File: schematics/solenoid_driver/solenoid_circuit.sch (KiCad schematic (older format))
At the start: 10 parts, among them Q1 Q_NPN_CBE, Q2 Q_PNP_CBE, Q3 Q_NMOS_GDS, U2 SFH617A-1

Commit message: created mtrix_controller project, updated schematic on solenoid_driver
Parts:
- D1: value D_Schottky -> 1n5819
- Q1: value Q_NPN_CBE -> 2n3904
- Q2: value Q_PNP_CBE -> 2n3906
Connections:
- net labels added: +3.3V, Sig_in
- wire segments 34 -> 35
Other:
- moved on the sheet: R1
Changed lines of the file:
@@
 	5150 3300 5300 3300
 Wire Wire Line
-	5300 3100 5050 3100
+	5300 2400 5300 2650
 $Comp
 L Device:R R1
 U 1 1 613B2B01
-P 4900 3100
-F 0 "R1" V 4693 3100 50  0000 C CNN
-F 1 "R" V 4784 3100 50  0000 C CNN
-F 2 "" V 4830 3100 50  0001 C CNN
-F 3 "~" H 4900 3100 50  0001 C CNN
-	1    4900 3100
-	0    1    1    0
-$EndComp
-Wire Wire Line
-	4600 3100 4750 3100
+P 5300 2800
+F 0 "R1" V 5093 2800 50  0000 C CNN
+F 1 "R" V 5184 2800 50  0000 C CNN
+F 2 "" V 5230 2800 50  0001 C CNN
+F 3 "~" H 5300 2800 50  0001 C CNN
+	1    5300 2800
+	1    0    0    -1
+$EndComp
+Wire Wire Line
+	5300 3100 5300 2950
 $Comp
 L power:GND #PWR010
@@
 P 7000 2600
 F 0 "Q1" H 7191 2646 50  0000 L CNN
-F 1 "Q_NPN_CBE" H 7191 2555 50  0000 L CNN
+F 1 "2n3904" H 7200 2550 50  0000 L CNN
 F 2 "" H 7200 2700 50  0001 C CNN
 F 3 "~" H 7000 2600 50  0001 C CNN
@@
 P 7000 3100
 F 0 "Q2" H 7190 3054 50  0000 L CNN
-F 1 "Q_PNP_CBE" H 7190 3145 50  0000 L CNN
+F 1 "2n3906" H 7190 3145 50  0000 L CNN
 F 2 "" H 7200 3200 50  0001 C CNN
 F 3 "~" H 7000 3100 50  0001 C CNN
@@
 U 1 1 613B2B48
 P 7600 2850
-F 0 "R4" V 7393 2850 50  0000 C CNN
-F 1 "R" V 7484 2850 50  0000 C CNN
+F 0 "R4" V 7500 2900 50  0000 C CNN
+F 1 "R" V 7700 2900 50  0000 C CNN
 F 2 "" V 7530 2850 50  0001 C CNN
 F 3 "~" H 7600 2850 50  0001 C CNN
@@
 Wire Wire Line
 	8150 3050 8150 3550
-Wire Wire Line
-	7850 2850 7800 2850
 $Comp
 L Device:L_Core_Ferrite L1
@@
 P 8950 2200
 F 0 "D1" V 8904 2280 50  0000 L CNN
-F 1 "D_Schottky" V 8995 2280 50  0000 L CNN
+F 1 "1n5819" V 8995 2280 50  0000 L CNN
 F 2 "" H 8950 2200 50  0001 C CNN
 F 3 "~" H 8950 2200 50  0001 C CNN
@@
 Text Notes 4300 1750 0    50   ~ 0
 Solenoid driver circuit: \nmosfet push-pull circuit
+Wire Wire Line
+	7750 2850 7850 2850
+$Comp
+L power:+3.3V #PWR?
+U 1 1 614B4CD8
+P 5300 2400
+F 0 "#PWR?" H 5300 2250 50  0001 C CNN
+F 1 "+3.3V" H 5315 2573 50  0000 C CNN
+F 2 "" H 5300 2400 50  0001 C CNN
+F 3 "" H 5300 2400 50  0001 C CNN
+	1    5300 2400
+	1    0    0    -1
+$EndComp
+Wire Wire Line
+	4700 3100 5300 3100
+Connection ~ 5300 3100
+Text HLabel 4700 3100 0    50   Input ~ 0
+Sig_in
 $EndSCHEMATC

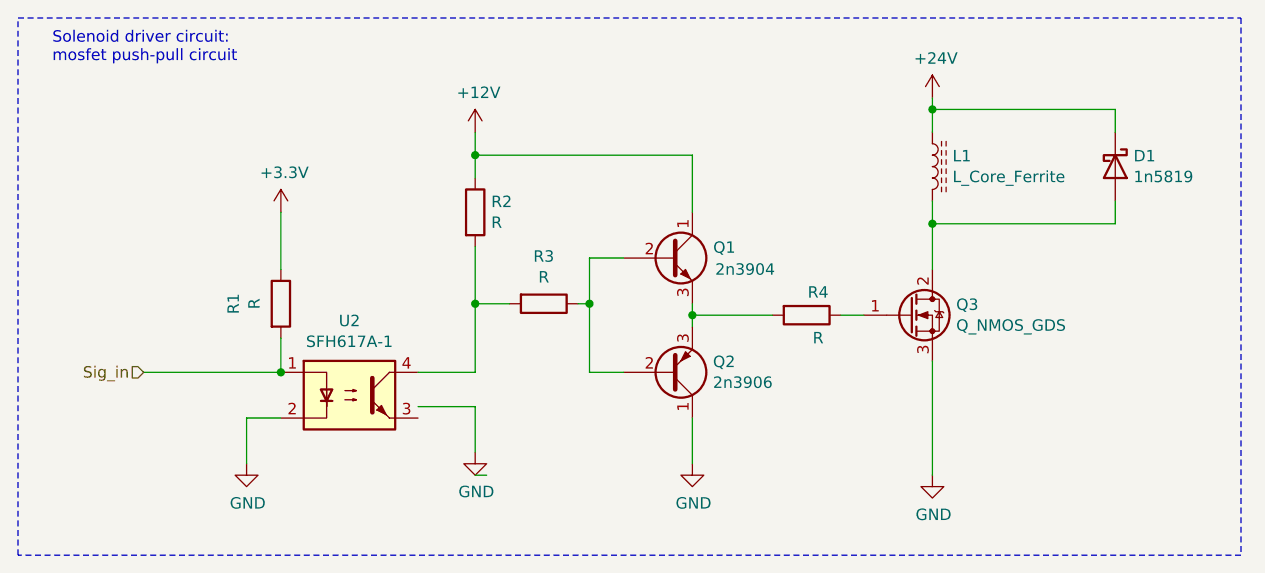
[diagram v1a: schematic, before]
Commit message: updated schematic: resistor value, added workspace for Waveforms Electronics Explorer
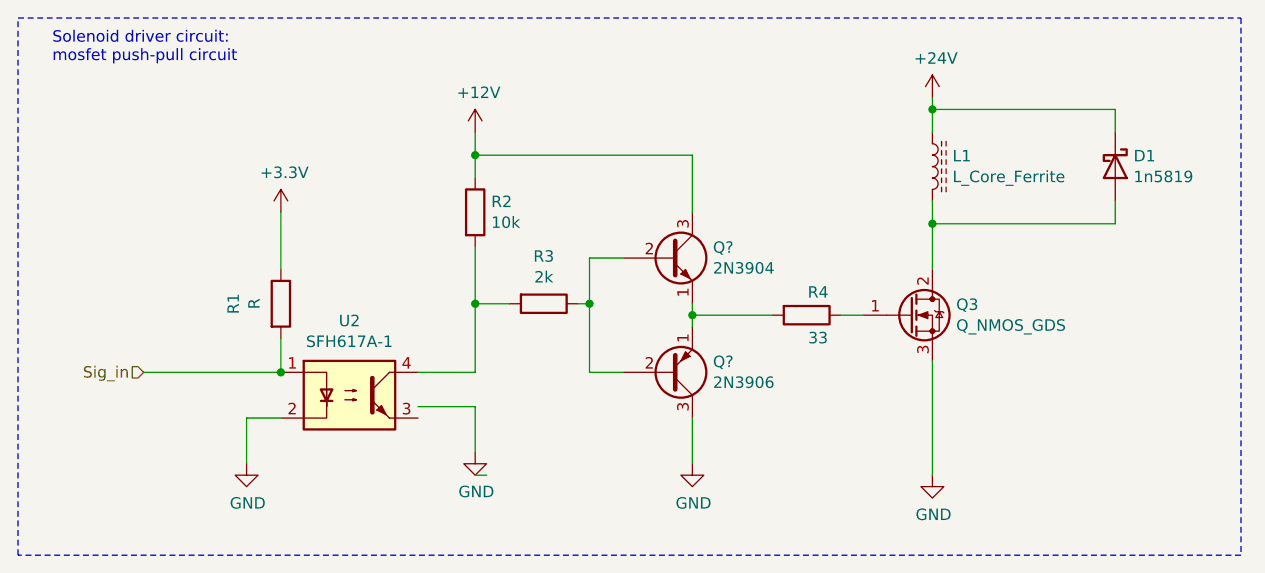
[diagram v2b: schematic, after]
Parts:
- removed Q1: 2n3904, symbol Device:Q_NPN_CBE
- removed Q2: 2n3906, symbol Device:Q_PNP_CBE
- added Q?: 2N3904, symbol Device:Q_NPN_EBC
- added Q?: 2N3906, symbol Device:Q_PNP_EBC
- R2: value R -> 10k
- R3: value R -> 2k
- R4: value R -> 33
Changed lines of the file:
@@
 P 6150 2400
 F 0 "R2" H 6220 2446 50  0000 L CNN
-F 1 "R" H 6220 2355 50  0000 L CNN
+F 1 "10k" H 6220 2355 50  0000 L CNN
 F 2 "" V 6080 2400 50  0001 C CNN
 F 3 "~" H 6150 2400 50  0001 C CNN
@@
 P 6450 2800
 F 0 "R3" V 6243 2800 50  0000 C CNN
-F 1 "R" V 6334 2800 50  0000 C CNN
+F 1 "2k" V 6334 2800 50  0000 C CNN
 F 2 "" V 6380 2800 50  0001 C CNN
 F 3 "~" H 6450 2800 50  0001 C CNN
 	1    6450 2800
 	0    1    1    0
-$EndComp
-$Comp
-L Device:Q_NPN_CBE Q1
-U 1 1 613B2B26
-P 7000 2600
-F 0 "Q1" H 7191 2646 50  0000 L CNN
-F 1 "2n3904" H 7200 2550 50  0000 L CNN
-F 2 "" H 7200 2700 50  0001 C CNN
-F 3 "~" H 7000 2600 50  0001 C CNN
-	1    7000 2600
-	1    0    0    -1
-$EndComp
-$Comp
-L Device:Q_PNP_CBE Q2
-U 1 1 613B2B2C
-P 7000 3100
-F 0 "Q2" H 7190 3054 50  0000 L CNN
-F 1 "2n3906" H 7190 3145 50  0000 L CNN
-F 2 "" H 7200 3200 50  0001 C CNN
-F 3 "~" H 7000 3100 50  0001 C CNN
-	1    7000 3100
-	1    0    0    1
 $EndComp
 Wire Wire Line
@@
 P 7600 2850
 F 0 "R4" V 7500 2900 50  0000 C CNN
-F 1 "R" V 7700 2900 50  0000 C CNN
+F 1 "33" V 7700 2900 50  0000 C CNN
 F 2 "" V 7530 2850 50  0001 C CNN
 F 3 "~" H 7600 2850 50  0001 C CNN
@@
 Text HLabel 4700 3100 0    50   Input ~ 0
 Sig_in
+$Comp
+L Device:Q_NPN_EBC Q?
+U 1 1 61538F3A
+P 7000 2600
+F 0 "Q?" H 7190 2646 50  0000 L CNN
+F 1 "2N3904" H 7190 2555 50  0000 L CNN
+F 2 "" H 7200 2700 50  0001 C CNN
+F 3 "~" H 7000 2600 50  0001 C CNN
+	1    7000 2600
+	1    0    0    -1
+$EndComp
+$Comp
+L Device:Q_PNP_EBC Q?
+U 1 1 61539B5E
+P 7000 3100
+F 0 "Q?" H 7190 3054 50  0000 L CNN
+F 1 "2N3906" H 7190 3145 50  0000 L CNN
+F 2 "" H 7200 3200 50  0001 C CNN
+F 3 "~" H 7000 3100 50  0001 C CNN
+	1    7000 3100
+	1    0    0    1
+$EndComp
 $EndSCHEMATC

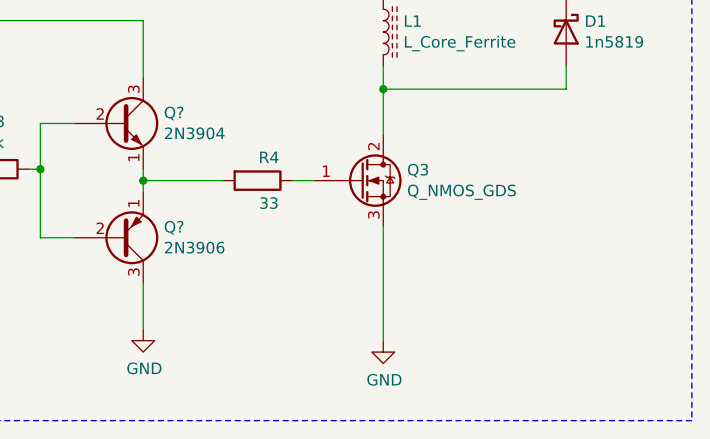
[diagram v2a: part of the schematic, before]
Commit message: updated schematics to add a op amp for current sensing
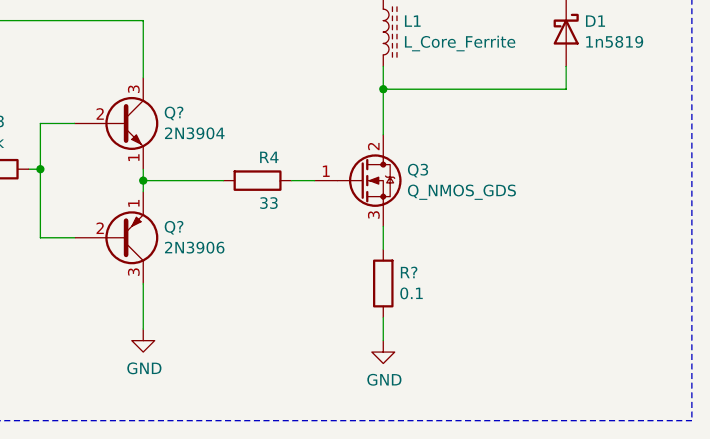
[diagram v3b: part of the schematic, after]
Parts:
- added R?: 0.1, symbol Device:R
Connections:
- wire segments 35 -> 36
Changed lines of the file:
@@
 	1    0    0    -1
 $EndComp
-Wire Wire Line
-	8150 3050 8150 3550
 $Comp
 L Device:L_Core_Ferrite L1
@@
 	1    0    0    1
 $EndComp
+$Comp
+L Device:R R?
+U 1 1 616C6F19
+P 8150 3300
+F 0 "R?" H 8080 3254 50  0000 R CNN
+F 1 "0.1" H 8080 3345 50  0000 R CNN
+F 2 "" V 8080 3300 50  0001 C CNN
+F 3 "~" H 8150 3300 50  0001 C CNN
+	1    8150 3300
+	-1   0    0    1
+$EndComp
+Wire Wire Line
+	8150 3450 8150 3550
+Wire Wire Line
+	8150 3150 8150 3050
 $EndSCHEMATC

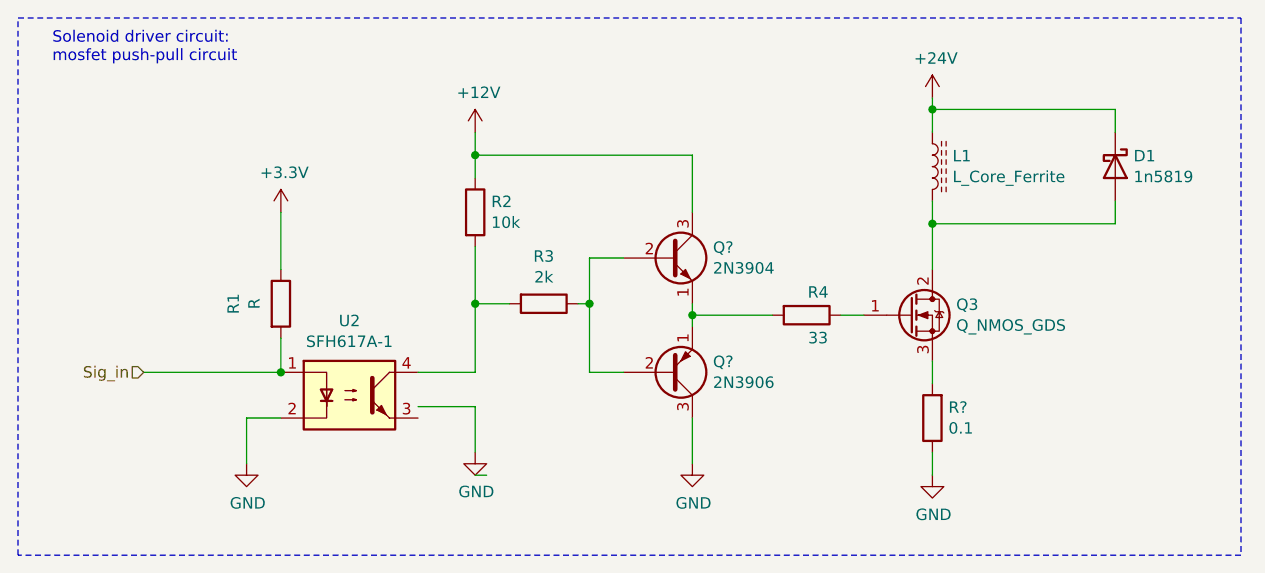
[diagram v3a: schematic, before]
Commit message: updated solenoid circuit with correct amplifier resitor values
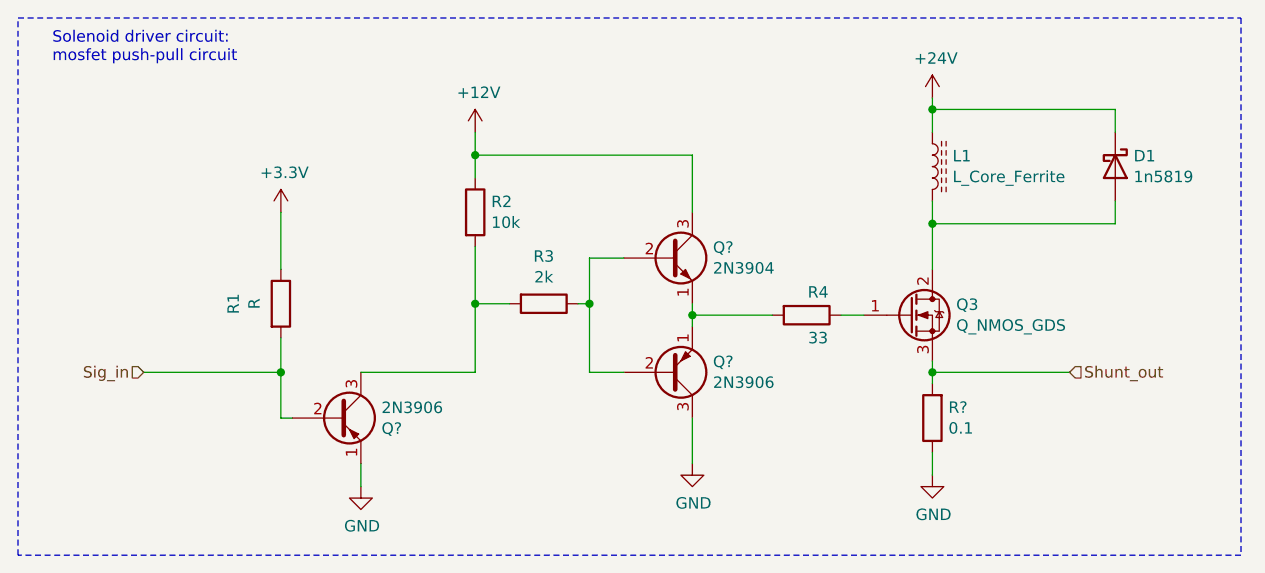
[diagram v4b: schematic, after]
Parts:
- removed U2: SFH617A-1, Package_DIP:DIP-4_W7.62mm, symbol Isolator:SFH617A-1
- added Q?: 2N3906, symbol Device:Q_PNP_EBC
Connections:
- net labels added: Shunt_out
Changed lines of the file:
@@
 Comment4 ""
 $EndDescr
-$Comp
-L Isolator:SFH617A-1 U2
-U 1 1 613B2AF2
-P 5600 3200
-F 0 "U2" H 5600 3525 50  0000 C CNN
-F 1 "SFH617A-1" H 5600 3434 50  0000 C CNN
-F 2 "Package_DIP:DIP-4_W7.62mm" H 5400 3000 50  0001 L CIN
-F 3 "http://www.vishay.com/docs/83740/sfh617a.pdf" H 5600 3200 50  0001 L CNN
-	1    5600 3200
-	1    0    0    -1
-$EndComp
-$Comp
-L power:GND #PWR08
-U 1 1 613B2AF8
-P 5150 3500
-F 0 "#PWR08" H 5150 3250 50  0001 C CNN
-F 1 "GND" H 5155 3327 50  0000 C CNN
-F 2 "" H 5150 3500 50  0001 C CNN
-F 3 "" H 5150 3500 50  0001 C CNN
-	1    5150 3500
-	1    0    0    -1
-$EndComp
-Wire Wire Line
-	5150 3500 5150 3300
-Wire Wire Line
-	5150 3300 5300 3300
 Wire Wire Line
 	5300 2400 5300 2650
-$Comp
-L Device:R R1
-U 1 1 613B2B01
-P 5300 2800
-F 0 "R1" V 5093 2800 50  0000 C CNN
-F 1 "R" V 5184 2800 50  0000 C CNN
-F 2 "" V 5230 2800 50  0001 C CNN
-F 3 "~" H 5300 2800 50  0001 C CNN
-	1    5300 2800
-	1    0    0    -1
-$EndComp
 Wire Wire Line
 	5300 3100 5300 2950
@@
 L power:GND #PWR010
 U 1 1 613B2B09
-P 6150 3450
-F 0 "#PWR010" H 6150 3200 50  0001 C CNN
-F 1 "GND" H 6155 3277 50  0000 C CNN
-F 2 "" H 6150 3450 50  0001 C CNN
-F 3 "" H 6150 3450 50  0001 C CNN
-	1    6150 3450
-	1    0    0    -1
-$EndComp
-Wire Wire Line
-	6150 3450 6150 3250
-Wire Wire Line
-	6150 3250 5900 3250
+P 5650 3600
+F 0 "#PWR010" H 5650 3350 50  0001 C CNN
+F 1 "GND" H 5655 3427 50  0000 C CNN
+F 2 "" H 5650 3600 50  0001 C CNN
+F 3 "" H 5650 3600 50  0001 C CNN
+	1    5650 3600
+	1    0    0    -1
+$EndComp
 $Comp
 L power:+12V #PWR09
@@
 Wire Wire Line
 	6150 2550 6150 2800
-Wire Wire Line
-	6150 3100 5900 3100
 Wire Wire Line
 	6150 2050 6150 2150
@@
 $EndComp
 Wire Wire Line
-	6200 3550 6150 3550
-Wire Wire Line
 	7100 3500 7100 3300
 Wire Wire Line
@@
 Wire Wire Line
 	4700 3100 5300 3100
-Connection ~ 5300 3100
 Text HLabel 4700 3100 0    50   Input ~ 0
 Sig_in
@@
 	8150 3450 8150 3550
 Wire Wire Line
-	8150 3150 8150 3050
+	8150 3150 8150 3100
+Text HLabel 8750 3100 2    50   Input ~ 0
+Shunt_out
+Wire Wire Line
+	8750 3100 8150 3100
+Connection ~ 8150 3100
+Wire Wire Line
+	8150 3100 8150 3050
+$Comp
+L Device:R R1
+U 1 1 613B2B01
+P 5300 2800
+F 0 "R1" V 5093 2800 50  0000 C CNN
+F 1 "R" V 5184 2800 50  0000 C CNN
+F 2 "" V 5230 2800 50  0001 C CNN
+F 3 "~" H 5300 2800 50  0001 C CNN
+	1    5300 2800
+	1    0    0    -1
+$EndComp
+$Comp
+L Device:Q_PNP_EBC Q?
+U 1 1 617048FD
+P 5550 3300
+F 0 "Q?" H 5740 3254 50  0000 L CNN
+F 1 "2N3906" H 5740 3345 50  0000 L CNN
+F 2 "" H 5750 3400 50  0001 C CNN
+F 3 "~" H 5550 3300 50  0001 C CNN
+	1    5550 3300
+	1    0    0    -1
+$EndComp
+Wire Wire Line
+	5650 3600 5650 3500
+Wire Wire Line
+	5650 3100 6150 3100
+Wire Wire Line
+	5300 3100 5300 3300
+Wire Wire Line
+	5300 3300 5350 3300
+Connection ~ 5300 3100
 $EndSCHEMATC
